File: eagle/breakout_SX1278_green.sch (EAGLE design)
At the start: 20 parts, among them X1 734120110

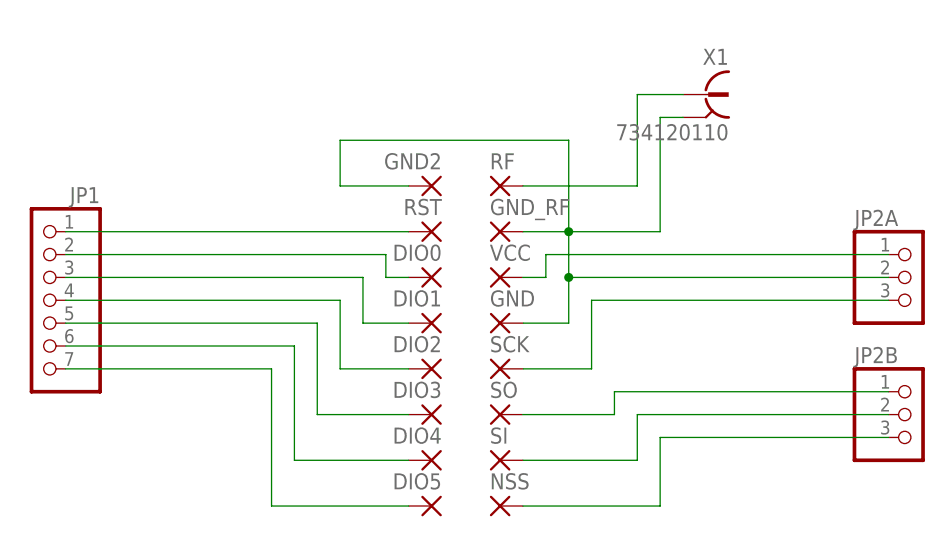
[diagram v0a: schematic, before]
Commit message: Major layout update, read details
The layouts of shield and all breakout boards were changed to match the new multiprotocol standard.
IMPORTANT: The new shield is NOT compatible with the old breakout boards!
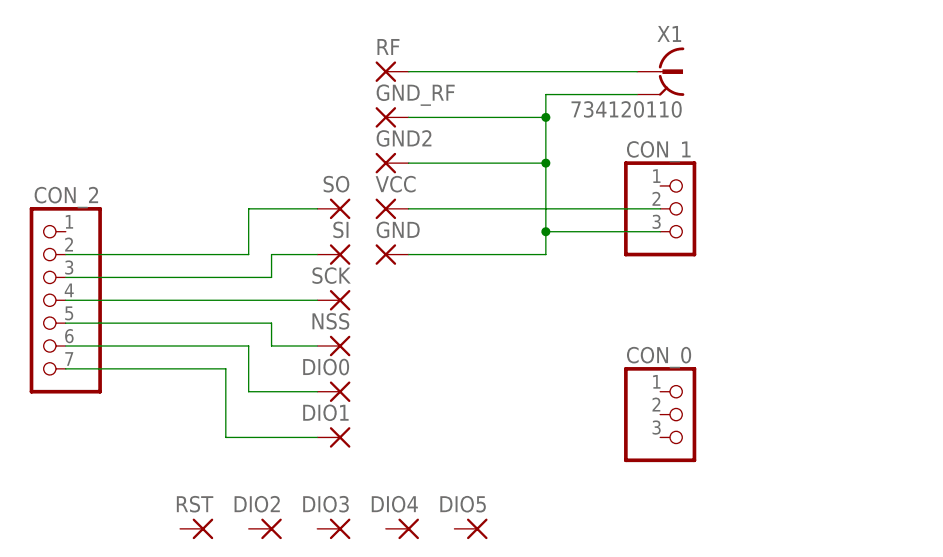
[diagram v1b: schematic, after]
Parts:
- removed JP2A, JP2B: (no value), pinhead:PINHD-1X3
- added CON_0, CON_1: (no value), pinhead:PINHD-1X3
- renumbered JP1 to CON_2
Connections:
- removed net 3.3V: JP2A.1, VCC.P
- removed net DIO2: CON_2.4, DIO2.P
- removed net DIO3: CON_2.5, DIO3.P
- removed net DIO4: CON_2.6, DIO4.P
- removed net DIO5: CON_2.7, DIO5.P
- removed net RESET: CON_2.1, RST.P
- new net VCC: CON_1.2, VCC.P
- net DIO0: now also CON_2.6; no longer CON_2.2
- net DIO1: now also CON_2.7; no longer CON_2.3
- net GND: now also CON_1.3; no longer JP2A.2
- net MISO: now also CON_2.2; no longer JP2B.1
- net MOSI: now also CON_2.3; no longer JP2B.2
- net NSS: now also CON_2.5; no longer JP2B.3
- net SCK: now also CON_2.4; no longer JP2A.3
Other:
- moved on the sheet: DIO0, DIO1, DIO2, DIO3, DIO4, DIO5, GND, GND2, GND_RF, NSS, RF, RST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

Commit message: Release 1.0
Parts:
- renumbered VCC to 3.3V
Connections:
- net VCC renamed 3.3V
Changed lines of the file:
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@@
 <setting verticaltext="up"/>
 </settings>
-<grid distance="0.1" unitdist="inch" unit="inch" style="lines" multiple="1" display="yes" altdistance="0.01" altunitdist="inch" altunit="inch"/>
+<grid distance="0.1" unitdist="inch" unit="inch" style="lines" multiple="1" display="no" altdistance="0.01" altunitdist="inch" altunit="inch"/>
 <layers>
 <layer number="1" name="Top" color="4" fill="1" visible="no" active="no"/>
@@
 <part name="GND_RF" library="wirepad" deviceset="SMD2" device=""/>
 <part name="RF" library="wirepad" deviceset="SMD2" device=""/>
-<part name="VCC" library="wirepad" deviceset="SMD2" device=""/>
+<part name="3.3V" library="wirepad" deviceset="SMD2" device=""/>
 <part name="GND" library="wirepad" deviceset="SMD2" device=""/>
 <part name="SCK" library="wirepad" deviceset="SMD2" device=""/>
@@
 <instance part="GND_RF" gate="1" x="55.88" y="73.66"/>
 <instance part="RF" gate="1" x="55.88" y="78.74"/>
-<instance part="VCC" gate="1" x="55.88" y="63.5"/>
+<instance part="3.3V" gate="1" x="55.88" y="63.5"/>
 <instance part="GND" gate="1" x="55.88" y="58.42"/>
 <instance part="SCK" gate="1" x="50.8" y="53.34" rot="MR0"/>
@@
 </segment>
 </net>
-<net name="VCC" class="0">
+<net name="3.3V" class="0">
 <segment>
 <pinref part="CON_1" gate="A" pin="2"/>
-<pinref part="VCC" gate="1" pin="P"/>
+<pinref part="3.3V" gate="1" pin="P"/>
 <wire x1="86.36" y1="63.5" x2="58.42" y2="63.5" width="0.1524" layer="91"/>
 </segment>
